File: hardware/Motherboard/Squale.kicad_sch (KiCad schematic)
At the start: 0 parts

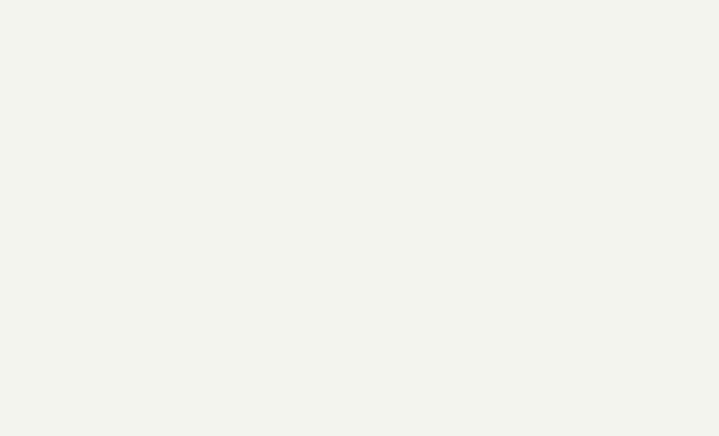
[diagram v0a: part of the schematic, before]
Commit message: Connectors footprint.
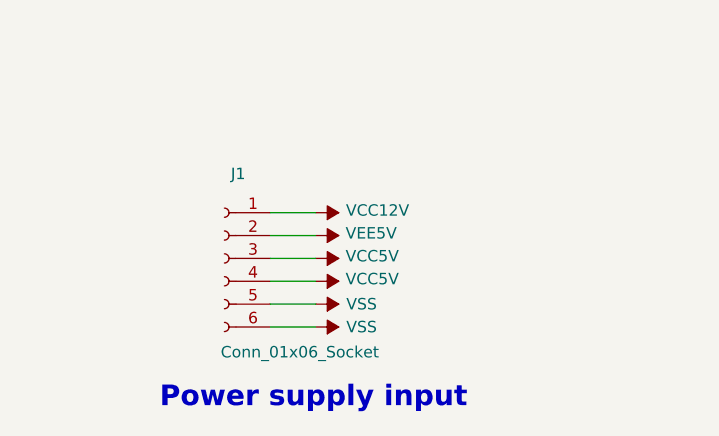
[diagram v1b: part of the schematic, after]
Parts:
- added J1: Conn_01x06_Socket, TerminalBlock_CUI:TerminalBlock_CUI_TB007-508-06_1x06_P5.08mm_Horizontal, symbol Connector:Conn_01x06_Socket
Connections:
- new net VCC12V: J1.1 (Pin_1)
- new net VCC5V: J1.3 (Pin_3), J1.4 (Pin_4)
- new net VEE5V: J1.2 (Pin_2)
- new net VSS: J1.5 (Pin_5), J1.6 (Pin_6)
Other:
- note added: "Power supply input"

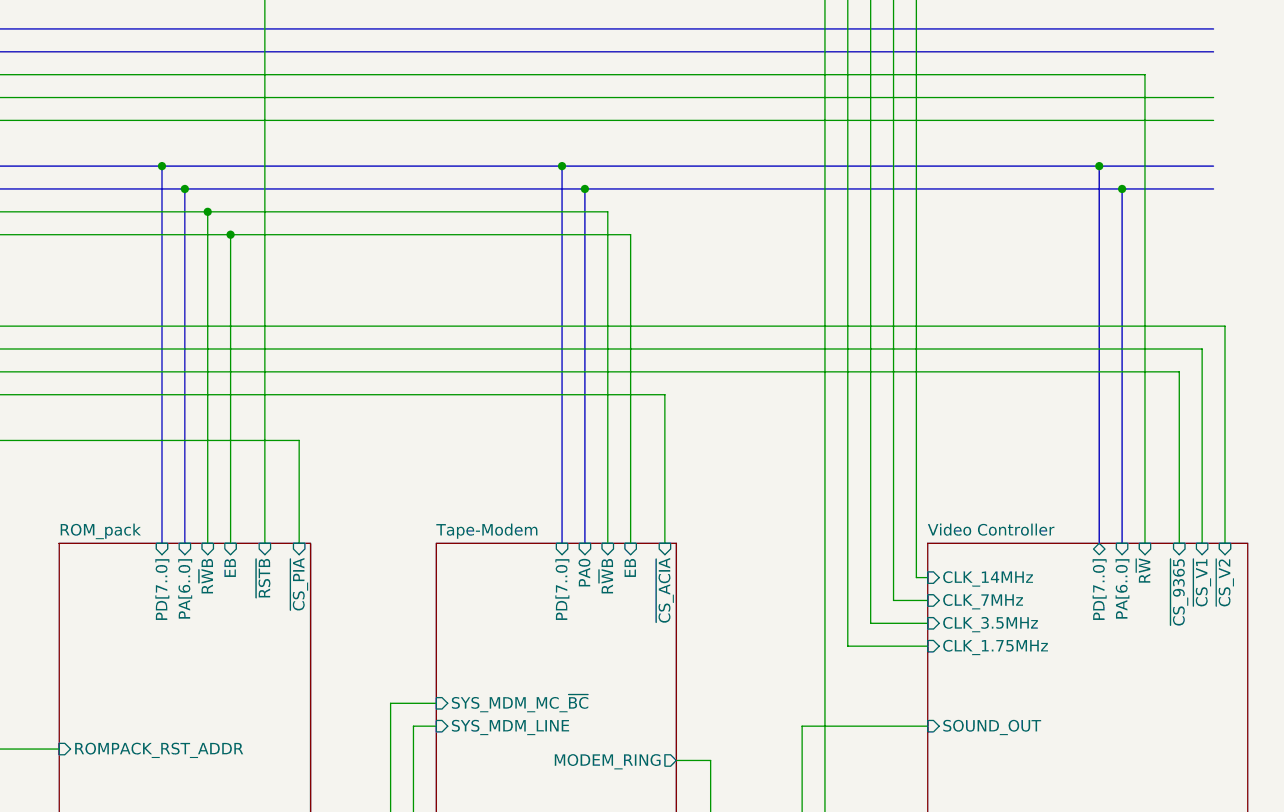
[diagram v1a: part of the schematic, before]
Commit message: connection fix + power line width.
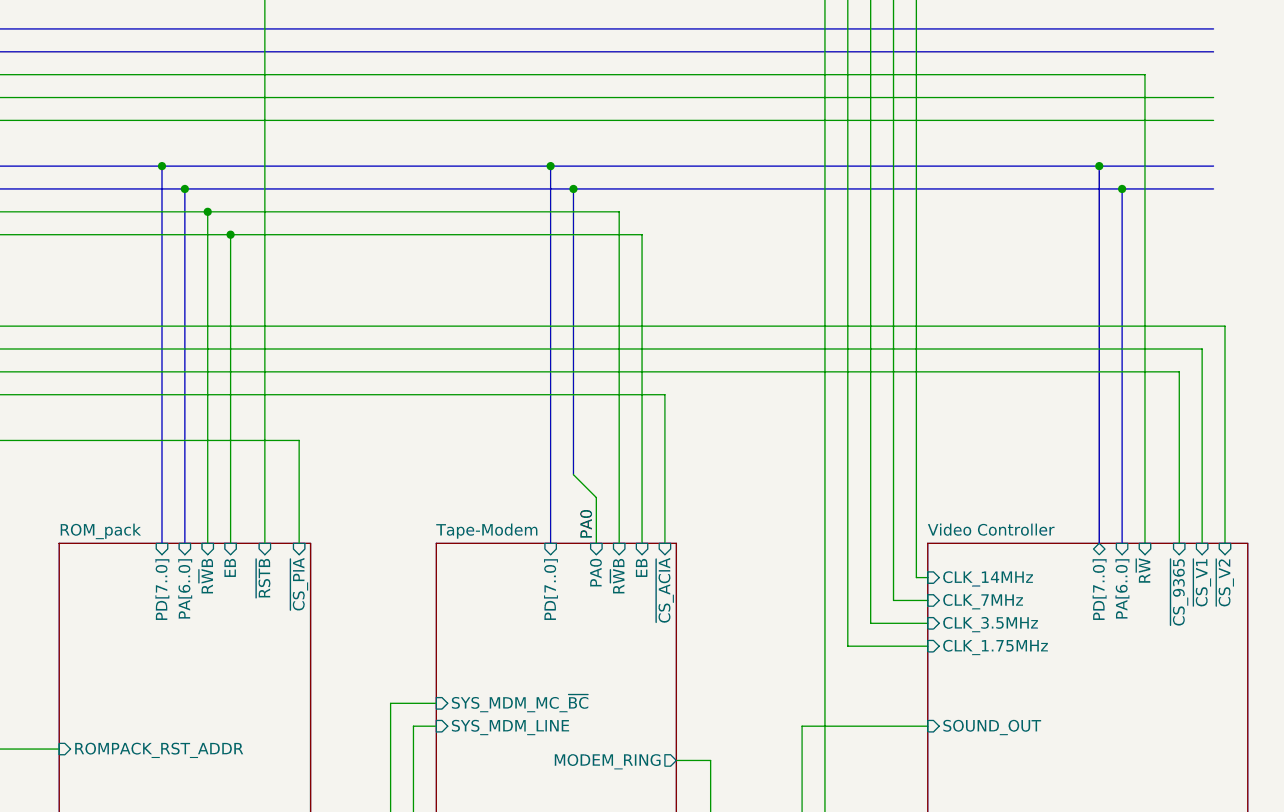
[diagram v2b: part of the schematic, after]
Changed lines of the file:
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@@
 	)
 	(junction
+		(at 326.39 100.33)
+		(diameter 0)
+		(color 0 0 0 0)
+	)
+	(junction
 		(at 191.77 107.95)
 		(diameter 0)
@@
 	)
 	(junction
-		(at 330.2 102.87)
-		(diameter 0)
-		(color 0 0 0 0)
-	)
-	(junction
 		(at 356.87 74.93)
 		(diameter 0)
@@
 	)
 	(junction
-		(at 327.66 100.33)
-		(diameter 0)
-		(color 0 0 0 0)
-	)
-	(junction
 		(at 389.89 102.87)
 		(diameter 0)
@@
 		(color 0 0 0 0)
 	)
+	(junction
+		(at 328.93 102.87)
+		(diameter 0)
+		(color 0 0 0 0)
+	)
+	(bus_entry
+		(at 328.93 134.62)
+		(size 2.54 2.54)
+		(stroke
+			(width 0)
+			(type default)
+		)
+	)
 	(bus_entry
 		(at 241.3 134.62)
@@
 	(wire
 		(pts
+			(xy 331.47 137.16) (xy 331.47 142.24)
+		)
+		(stroke
+			(width 0)
+			(type default)
+		)
+	)
+	(wire
+		(pts
 			(xy 46.99 256.54) (xy 41.91 256.54)
 		)
@@
 		)
 	)
+	(bus
+		(pts
+			(xy 328.93 102.87) (xy 389.89 102.87)
+		)
+		(stroke
+			(width 0)
+			(type default)
+		)
+	)
 	(wire
 		(pts
@@
 	(wire
 		(pts
-			(xy 332.74 142.24) (xy 332.74 105.41)
+			(xy 334.01 142.24) (xy 334.01 105.41)
 		)
 		(stroke
@@
 	(bus
 		(pts
-			(xy 327.66 100.33) (xy 327.66 142.24)
+			(xy 326.39 100.33) (xy 326.39 142.24)
 		)
 		(stroke
@@
 	(wire
 		(pts
-			(xy 290.83 107.95) (xy 335.28 107.95)
+			(xy 290.83 107.95) (xy 336.55 107.95)
 		)
 		(stroke
@@
 	(bus
 		(pts
-			(xy 330.2 102.87) (xy 330.2 142.24)
-		)
-		(stroke
-			(width 0)
-			(type default)
-		)
-	)
-	(bus
-		(pts
 			(xy 387.35 100.33) (xy 400.05 100.33)
 		)
@@
 		)
 	)
+	(bus
+		(pts
+			(xy 326.39 100.33) (xy 387.35 100.33)
+		)
+		(stroke
+			(width 0)
+			(type default)
+		)
+	)
 	(wire
 		(pts
@@
 	(wire
 		(pts
-			(xy 335.28 107.95) (xy 335.28 142.24)
+			(xy 336.55 107.95) (xy 336.55 142.24)
 		)
 		(stroke
@@
 	(bus
 		(pts
-			(xy 285.75 102.87) (xy 330.2 102.87)
+			(xy 285.75 102.87) (xy 328.93 102.87)
 		)
 		(stroke
@@
 		)
 	)
-	(bus
-		(pts
-			(xy 327.66 100.33) (xy 387.35 100.33)
-		)
-		(stroke
-			(width 0)
-			(type default)
-		)
-	)
 	(wire
 		(pts
@@
 	(bus
 		(pts
-			(xy 283.21 100.33) (xy 327.66 100.33)
+			(xy 283.21 100.33) (xy 326.39 100.33)
 		)
 		(stroke
@@
 	(wire
 		(pts
-			(xy 288.29 105.41) (xy 332.74 105.41)
+			(xy 288.29 105.41) (xy 334.01 105.41)
 		)
 		(stroke
@@
 	(bus
 		(pts
+			(xy 328.93 102.87) (xy 328.93 134.62)
+		)
+		(stroke
+			(width 0)
+			(type default)
+		)
+	)
+	(bus
+		(pts
 			(xy 241.3 87.63) (xy 241.3 134.62)
 		)
@@
 		)
 	)
-	(bus
-		(pts
-			(xy 330.2 102.87) (xy 389.89 102.87)
-		)
-		(stroke
-			(width 0)
-			(type default)
-		)
-	)
 	(wire
 		(pts
@@
 		)
 	)
+	(label "PA0"
+		(at 331.47 138.43 270)
+		(effects
+			(font
+				(size 1.27 1.27)
+			)
+			(justify right bottom)
+		)
+	)
 	(label "A[15..0]"
 		(at 62.23 87.63 0)
@@
 		)
 		(pin "PA0" input
-			(at 330.2 142.24 90)
+			(at 331.47 142.24 90)
 			(effects
 				(font
@@
 		)
 		(pin "EB" input
-			(at 335.28 142.24 90)
+			(at 336.55 142.24 90)
 			(effects
 				(font
@@
 		)
 		(pin "R~{W}B" input
-			(at 332.74 142.24 90)
+			(at 334.01 142.24 90)
 			(effects
 				(font
@@
 		)
 		(pin "PD[7..0]" input
-			(at 327.66 142.24 90)
+			(at 326.39 142.24 90)
 			(effects
 				(font

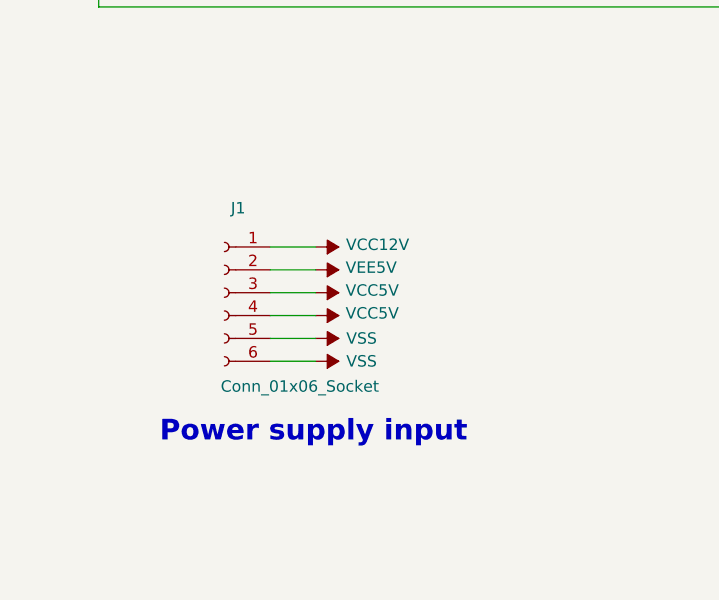
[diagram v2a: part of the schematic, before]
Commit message: add some descriptions / comments.
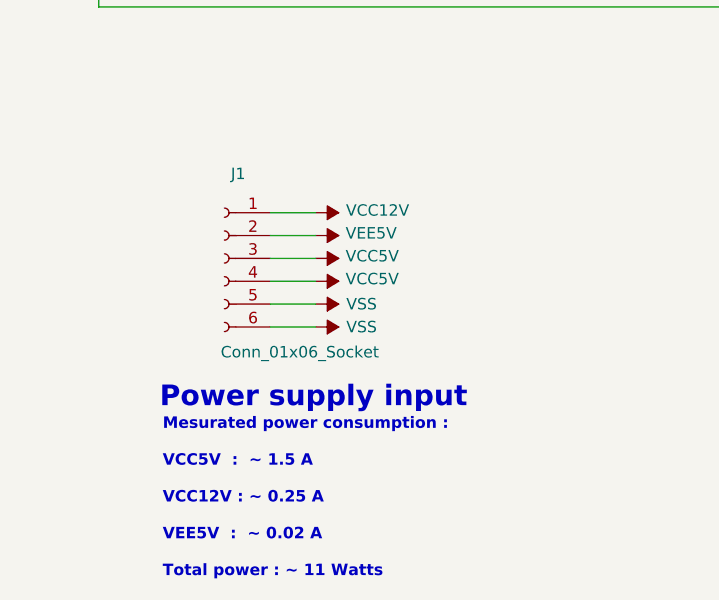
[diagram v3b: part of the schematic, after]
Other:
- note added: "Mesurated power consumption : VCC5V : ~ 1.5 A VCC12V : ~ 0.25 A VEE5V : ~ 0.02 A Total power : ~ 11 Watts"
- moved on the sheet: J1
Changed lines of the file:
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@@
 	(text "Power supply input"
 		(exclude_from_sim no)
-		(at 46.736 264.414 0)
+		(at 46.736 260.604 0)
 		(effects
 			(font
@@
 		)
 	)
+	(text "Mesurated power consumption :\n\nVCC5V  :  ~ 1.5 A\n\nVCC12V : ~ 0.25 A\n\nVEE5V  :  ~ 0.02 A\n\nTotal power : ~ 11 Watts\n"
+		(exclude_from_sim no)
+		(at 29.972 271.78 0)
+		(effects
+			(font
+				(size 1.27 1.27)
+				(thickness 0.254)
+				(bold yes)
+			)
+			(justify left)
+		)
+	)
 	(junction
 		(at 38.1 59.69)
@@
 	(wire
 		(pts
-			(xy 46.99 256.54) (xy 41.91 256.54)
+			(xy 46.99 252.73) (xy 41.91 252.73)
 		)
 		(stroke
@@
 	(wire
 		(pts
-			(xy 46.99 254) (xy 41.91 254)
+			(xy 46.99 250.19) (xy 41.91 250.19)
 		)
 		(stroke
@@
 	(wire
 		(pts
-			(xy 46.99 243.84) (xy 41.91 243.84)
+			(xy 46.99 240.03) (xy 41.91 240.03)
 		)
 		(stroke
@@
 	(wire
 		(pts
-			(xy 46.99 248.92) (xy 41.91 248.92)
+			(xy 46.99 245.11) (xy 41.91 245.11)
 		)
 		(stroke
@@
 	(wire
 		(pts
-			(xy 41.91 246.38) (xy 46.99 246.38)
+			(xy 41.91 242.57) (xy 46.99 242.57)
 		)
 		(stroke
@@
 	(wire
 		(pts
-			(xy 41.91 251.46) (xy 46.99 251.46)
+			(xy 41.91 247.65) (xy 46.99 247.65)
 		)
 		(stroke
@@
 	(symbol
 		(lib_id "power:VSS")
-		(at 46.99 256.54 270)
+		(at 46.99 252.73 270)
 		(unit 1)
 		(exclude_from_sim no)
@@
 		(dnp no)
 		(property "Reference" "#PWR0124"
-			(at 43.18 256.54 0)
+			(at 43.18 252.73 0)
 			(effects
 				(font
@@
 		)
 		(property "Value" "VSS"
-			(at 52.07 256.54 90)
+			(at 52.07 252.73 90)
 			(effects
 				(font
@@
 		)
 		(property "Footprint" ""
-			(at 46.99 256.54 0)
+			(at 46.99 252.73 0)
 			(effects
 				(font
@@
 		)
 		(property "Datasheet" ""
-			(at 46.99 256.54 0)
+			(at 46.99 252.73 0)
 			(effects
 				(font
@@
 		)
 		(property "Description" "Power symbol creates a global label with name \"VSS\""
-			(at 46.99 256.54 0)
+			(at 46.99 252.73 0)
 			(effects
 				(font
@@
 	(symbol
 		(lib_id "power:VSS")
-		(at 46.99 243.84 270)
+		(at 46.99 240.03 270)
 		(unit 1)
 		(exclude_from_sim no)
@@
 		(dnp no)
 		(property "Reference" "#PWR0380"
-			(at 43.18 243.84 0)
+			(at 43.18 240.03 0)
 			(effects
 				(font
@@
 		)
 		(property "Value" "VCC12V"
-			(at 53.848 243.586 90)
+			(at 53.848 239.776 90)
 			(effects
 				(font
@@
 		)
 		(property "Footprint" ""
-			(at 46.99 243.84 0)
+			(at 46.99 240.03 0)
 			(effects
 				(font
@@
 		)
 		(property "Datasheet" ""
-			(at 46.99 243.84 0)
+			(at 46.99 240.03 0)
 			(effects
 				(font
@@
 		)
 		(property "Description" "Power symbol creates a global label with name \"VSS\""
-			(at 46.99 243.84 0)
+			(at 46.99 240.03 0)
 			(effects
 				(font
@@
 	(symbol
 		(lib_id "power:VSS")
-		(at 46.99 251.46 270)
+		(at 46.99 247.65 270)
 		(unit 1)
 		(exclude_from_sim no)
@@
 		(dnp no)
 		(property "Reference" "#PWR0379"
-			(at 43.18 251.46 0)
+			(at 43.18 247.65 0)
 			(effects
 				(font
@@
 		)
 		(property "Value" "VCC5V"
-			(at 50.292 251.206 90)
+			(at 50.292 247.396 90)
 			(effects
 				(font
@@
 		)
 		(property "Footprint" ""
-			(at 46.99 251.46 0)
+			(at 46.99 247.65 0)
 			(effects
 				(font
@@
 		)
 		(property "Datasheet" ""
-			(at 46.99 251.46 0)
+			(at 46.99 247.65 0)
 			(effects
 				(font
@@
 		)
 		(property "Description" "Power symbol creates a global label with name \"VSS\""
-			(at 46.99 251.46 0)
+			(at 46.99 247.65 0)
 			(effects
 				(font
@@
 	(symbol
 		(lib_id "power:VSS")
-		(at 46.99 254 270)
+		(at 46.99 250.19 270)
 		(unit 1)
 		(exclude_from_sim no)
@@
 		(dnp no)
 		(property "Reference" "#PWR0150"
-			(at 43.18 254 0)
+			(at 43.18 250.19 0)
 			(effects
 				(font
@@
 		)
 		(property "Value" "VSS"
-			(at 52.07 254 90)
+			(at 52.07 250.19 90)
 			(effects
 				(font
@@
 		)
 		(property "Footprint" ""
-			(at 46.99 254 0)
+			(at 46.99 250.19 0)
 			(effects
 				(font
@@
 		)
 		(property "Datasheet" ""
-			(at 46.99 254 0)
+			(at 46.99 250.19 0)
 			(effects
 				(font
@@
 		)
 		(property "Description" "Power symbol creates a global label with name \"VSS\""
-			(at 46.99 254 0)
+			(at 46.99 250.19 0)
 			(effects
 				(font
@@
 	(symbol
 		(lib_id "power:VSS")
-		(at 46.99 248.92 270)
+		(at 46.99 245.11 270)
 		(unit 1)
 		(exclude_from_sim no)
@@
 		(dnp no)
 		(property "Reference" "#PWR0163"
-			(at 43.18 248.92 0)
+			(at 43.18 245.11 0)
 			(effects
 				(font
@@
 		)
 		(property "Value" "VCC5V"
-			(at 50.292 248.666 90)
+			(at 50.292 244.856 90)
 			(effects
 				(font
@@
 		)
 		(property "Footprint" ""
-			(at 46.99 248.92 0)
+			(at 46.99 245.11 0)
 			(effects
 				(font
@@
 		)
 		(property "Datasheet" ""
-			(at 46.99 248.92 0)
+			(at 46.99 245.11 0)
 			(effects
 				(font
@@
 		)
 		(property "Description" "Power symbol creates a global label with name \"VSS\""
-			(at 46.99 248.92 0)
+			(at 46.99 245.11 0)
 			(effects
 				(font
@@
 	(symbol
 		(lib_id "Connector:Conn_01x06_Socket")
-		(at 36.83 248.92 0)
+		(at 36.83 245.11 0)
 		(mirror y)
 		(unit 1)
@@
 		(dnp no)
 		(property "Reference" "J1"
-			(at 38.354 239.522 0)
+			(at 38.354 235.712 0)
 			(effects
 				(font
@@
 		)
 		(property "Value" "Conn_01x06_Socket"
-			(at 45.212 259.334 0)
+			(at 45.212 255.524 0)
 			(effects
 				(font
@@
 		)
 		(property "Footprint" "TerminalBlock_CUI:TerminalBlock_CUI_TB007-508-06_1x06_P5.08mm_Horizontal"
-			(at 36.83 248.92 0)
+			(at 36.83 245.11 0)
 			(effects
 				(font
@@
 		)
 		(property "Datasheet" "~"
-			(at 36.83 248.92 0)
+			(at 36.83 245.11 0)
 			(effects
 				(font
@@
 		)
 		(property "Description" "Generic connector, single row, 01x06, script generated"
-			(at 36.83 248.92 0)
+			(at 36.83 245.11 0)
 			(effects
 				(font
@@
 	(symbol
 		(lib_id "power:VSS")
-		(at 46.99 246.38 270)
+		(at 46.99 242.57 270)
 		(unit 1)
 		(exclude_from_sim no)
@@
 		(dnp no)
 		(property "Reference" "#PWR0381"
-			(at 43.18 246.38 0)
+			(at 43.18 242.57 0)
 			(effects
 				(font
@@
 		)
 		(property "Value" "VEE5V"
-			(at 50.292 246.126 90)
+			(at 50.292 242.316 90)
 			(effects
 				(font
@@
 		)
 		(property "Footprint" ""
-			(at 46.99 246.38 0)
+			(at 46.99 242.57 0)
 			(effects
 				(font
@@
 		)
 		(property "Datasheet" ""
-			(at 46.99 246.38 0)
+			(at 46.99 242.57 0)
 			(effects
 				(font
@@
 		)
 		(property "Description" "Power symbol creates a global label with name \"VSS\""
-			(at 46.99 246.38 0)
-			(effects
-				(font
+			(at 46.99 242.57 0)
+			(effects
+				(font
